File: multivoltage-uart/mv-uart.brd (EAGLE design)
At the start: 37.9 x 33.5 mm, 38 parts, among them SW1 DIP_SP6T, U1 IP4234CZ6, U2 CP2105-GM, U3 LDO_SHD_ADJ-AP2127K-ADJ, X1 MINI-USB-SHIELD-UX60-MB-5ST

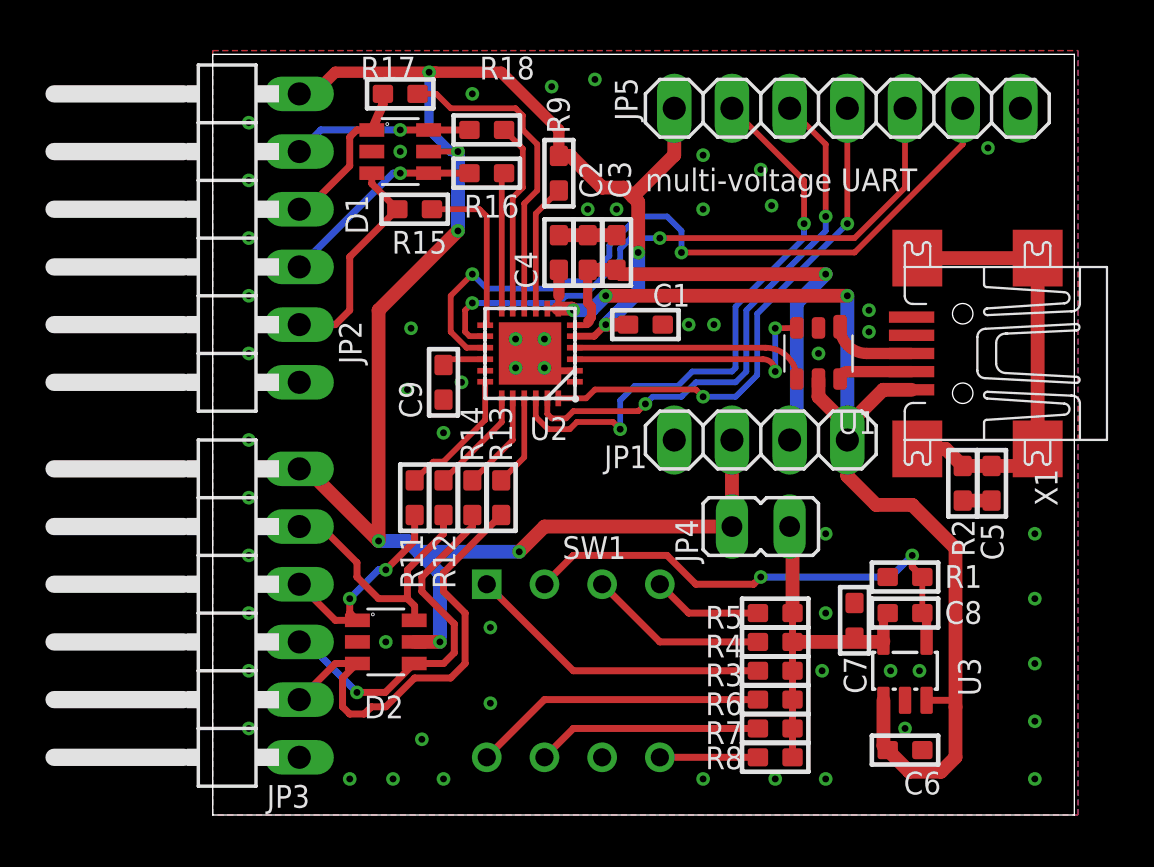
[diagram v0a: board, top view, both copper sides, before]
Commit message: mvuart: align JP2 in 0.1' grid with JP3 (solves OSM#3037)
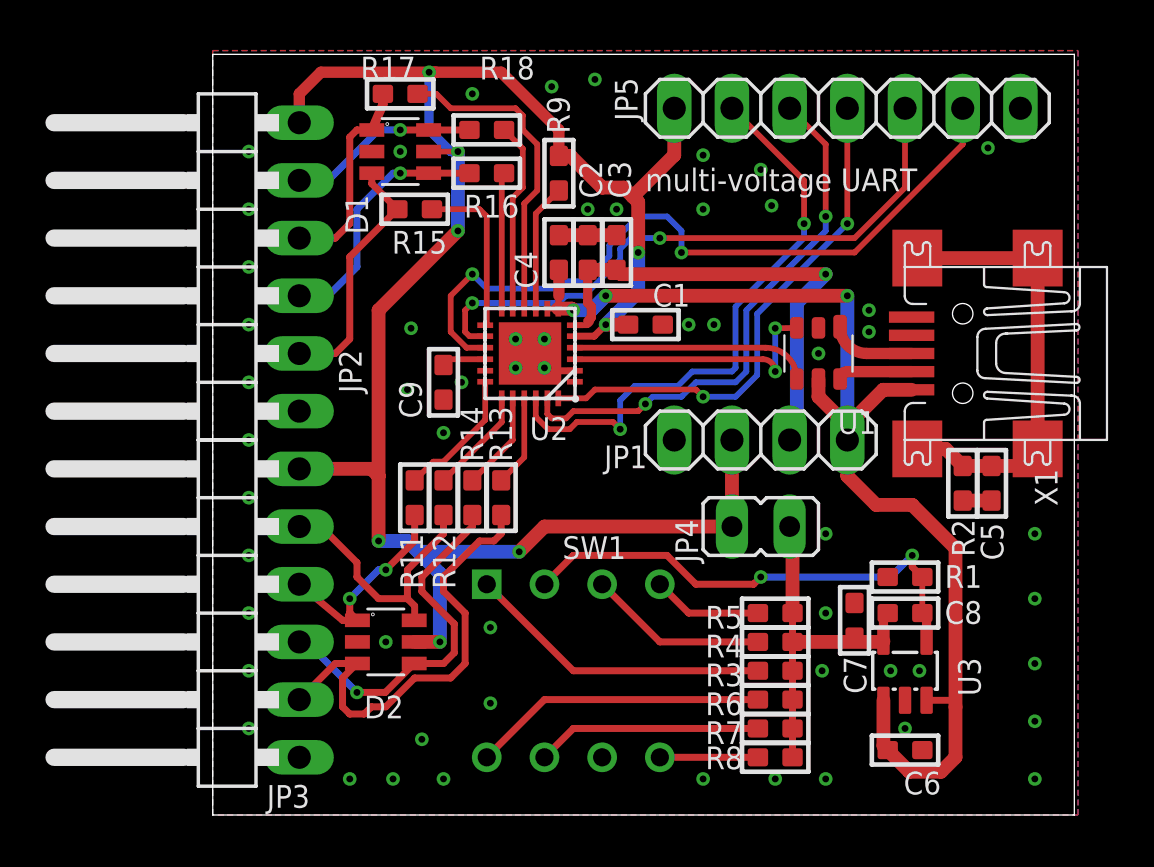
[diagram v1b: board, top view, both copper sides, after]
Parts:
- moved JP2 1.27 mm to (0.00, 24.1)
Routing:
- net CTS_ECI: track 7.08 -> 9.09 mm
- net RXD_ECI: track 9.20 -> 11.2 mm
- net TXD_ECI: track 9.85 -> 11.1 mm
- net RTS_ECI: track 7.89 -> 8.42 mm
